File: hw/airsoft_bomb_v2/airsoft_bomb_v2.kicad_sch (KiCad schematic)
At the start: 43 parts, among them J1 Conn_01x10_Pin, J2 Conn_01x16_Pin, J3 BTN_R, J4 BTN_Y, J5 SIREN, J6 Conn_01x02_Socket, Q2 AO3400A, Q4 AO3400A, Q5 AO3400A, U1 PCF8574, U2 PCF8574, U4 LM317_SOT-223

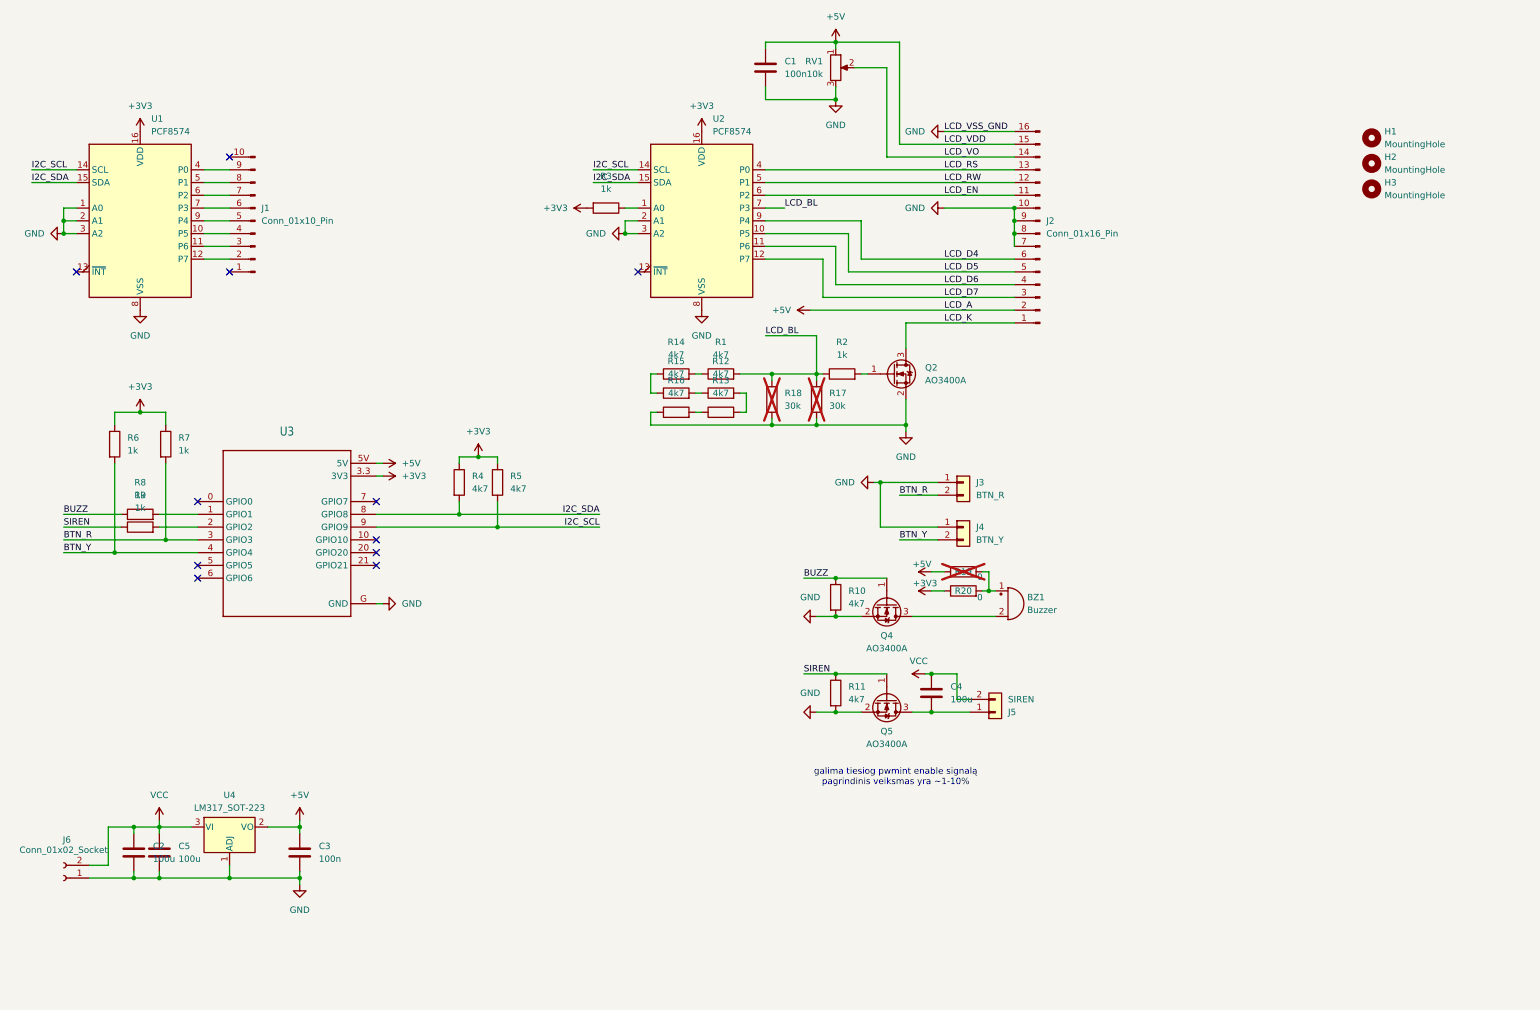
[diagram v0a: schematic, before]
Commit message: add kibot.sh and required fixes
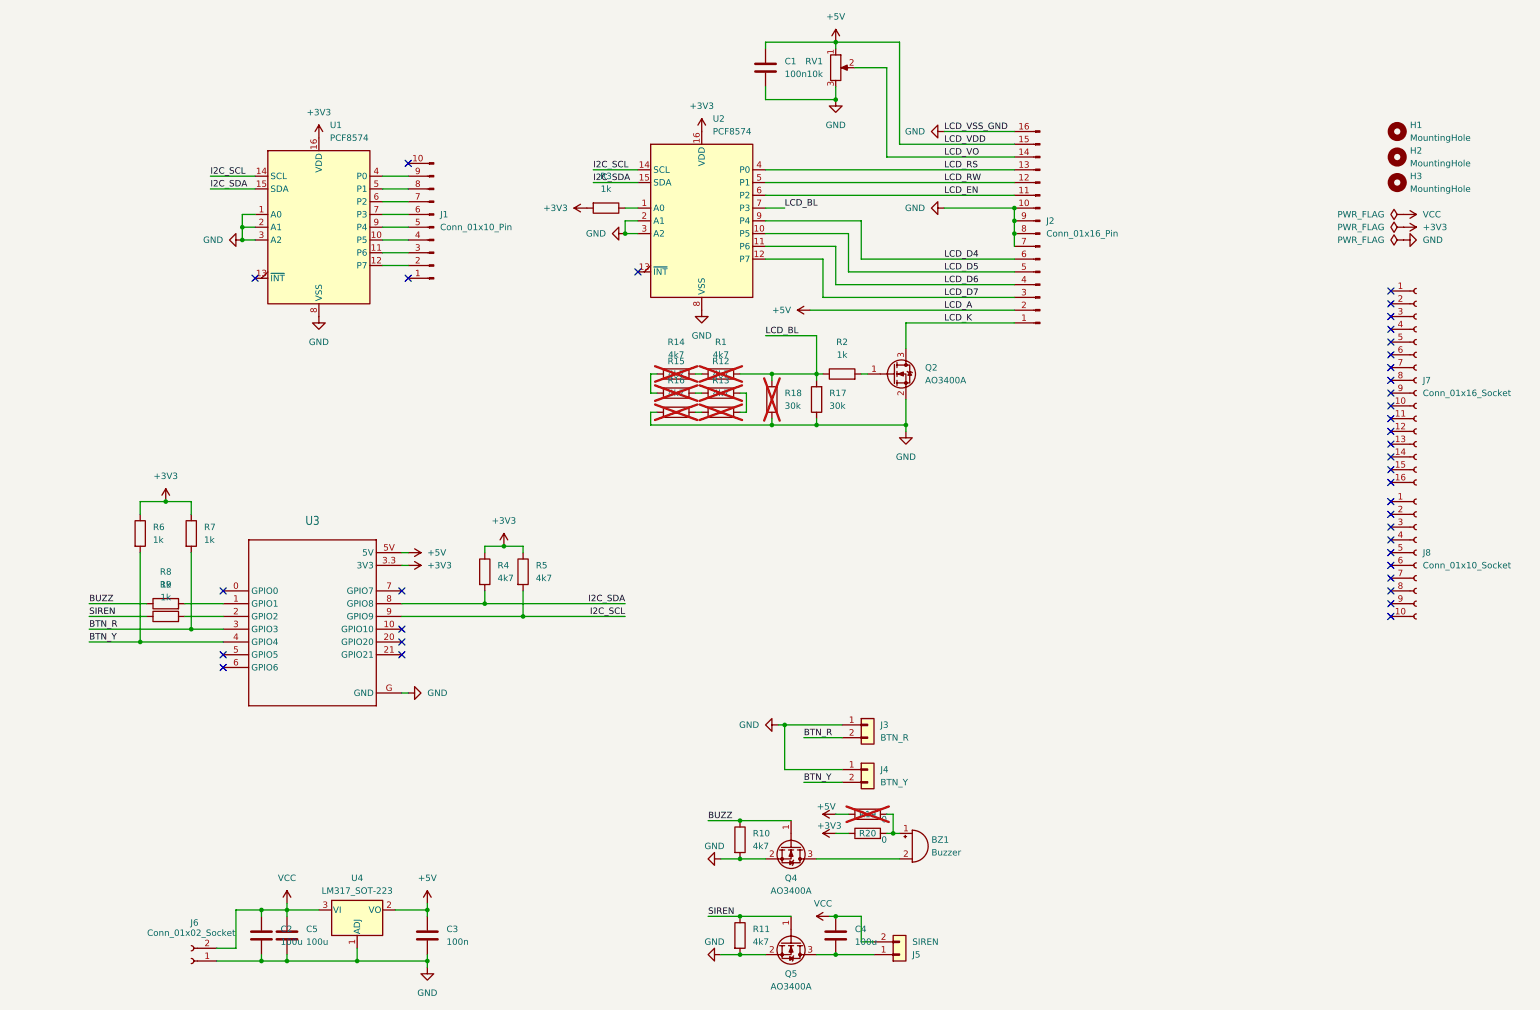
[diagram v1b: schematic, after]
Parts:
- added J7: Conn_01x16_Socket, Connector_PinHeader_2.54mm:PinHeader_1x16_P2.54mm_Horizontal, symbol Connector:Conn_01x16_Socket
- added J8: Conn_01x10_Socket, Connector_PinHeader_2.54mm:PinHeader_1x10_P2.54mm_Horizontal, symbol Connector:Conn_01x10_Socket
- R1, R12, R13, R14, R15, R16: now not fitted; now left out of the parts list
- R17: now fitted; now in the parts list
- R19: now left out of the parts list
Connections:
- no-connect marks 11 -> 37
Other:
- note removed: "galima tiesiog pwmint enable signalą pagrindinis veiksmas yra ~1-10%"
- moved on the sheet: BZ1, C2, C3, C4, C5, H1, H2, H3, J1, J3, J4, J5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

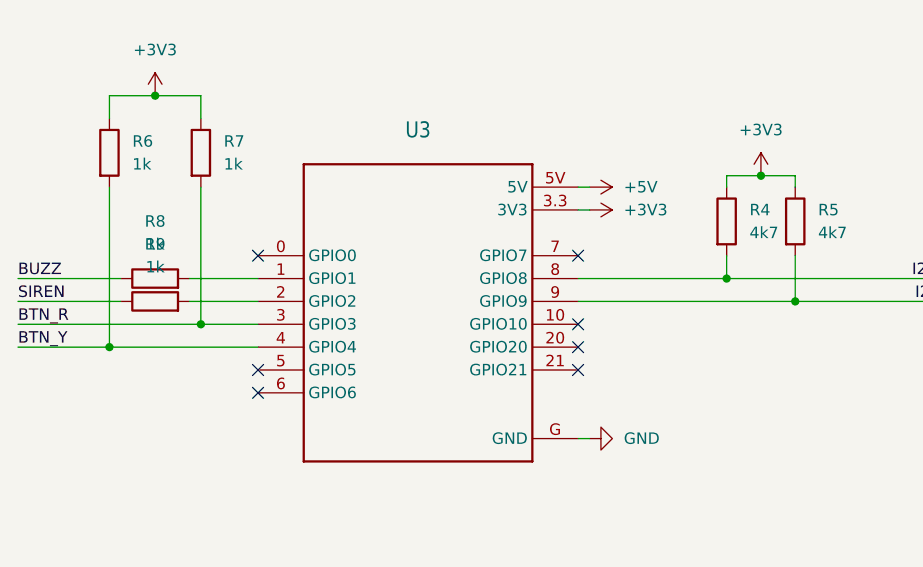
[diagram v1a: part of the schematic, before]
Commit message: move siren pin to something that is not high on boot
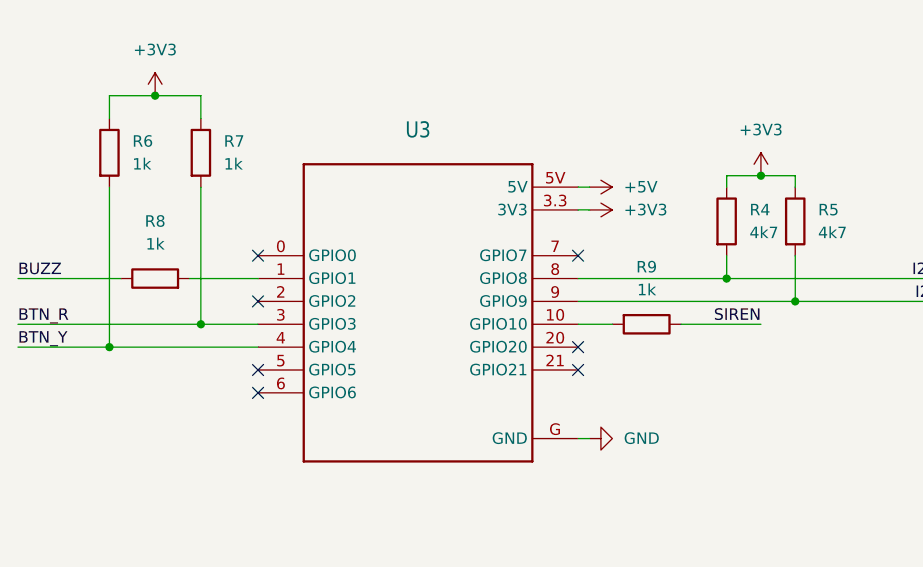
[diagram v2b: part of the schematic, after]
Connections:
- net at R9.2: now also U3.10 (GPIO10); no longer U3.2 (GPIO2)
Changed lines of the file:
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@@
 	)
 	(no_connect
-		(at 105.41 153.67)
-	)
-	(no_connect
 		(at 69.85 158.75)
 	)
@@
 	)
 	(no_connect
+		(at 69.85 151.13)
+	)
+	(no_connect
 		(at 302.26 116.84)
 	)
@@
 	(wire
 		(pts
+			(xy 116.84 153.67) (xy 125.73 153.67)
+		)
+		(stroke
+			(width 0)
+			(type default)
+		)
+	)
+	(wire
+		(pts
 			(xy 227.33 74.93) (xy 227.33 77.47)
 		)
@@
 	(wire
 		(pts
+			(xy 105.41 153.67) (xy 109.22 153.67)
+		)
+		(stroke
+			(width 0)
+			(type default)
+		)
+	)
+	(wire
+		(pts
 			(xy 149.86 148.59) (xy 121.92 148.59)
 		)
@@
 	(wire
 		(pts
-			(xy 43.18 151.13) (xy 54.61 151.13)
-		)
-		(stroke
-			(width 0)
-			(type default)
-		)
-	)
-	(wire
-		(pts
 			(xy 43.18 156.21) (xy 53.34 156.21)
 		)
@@
 	(wire
 		(pts
-			(xy 62.23 151.13) (xy 69.85 151.13)
-		)
-		(stroke
-			(width 0)
-			(type default)
-		)
-	)
-	(wire
-		(pts
 			(xy 196.85 215.9) (xy 199.39 215.9)
 		)
@@
 		)
 	)
+	(label "SIREN"
+		(at 125.73 153.67 180)
+		(effects
+			(font
+				(size 1.27 1.27)
+			)
+			(justify right bottom)
+		)
+	)
 	(label "I2C_SDA"
 		(at 67.31 66.04 0)
@@
 		)
 	)
-	(label "SIREN"
-		(at 43.18 151.13 0)
-		(effects
-			(font
-				(size 1.27 1.27)
-			)
-			(justify left bottom)
-		)
-	)
 	(label "BTN_Y"
 		(at 185.42 184.15 0)
@@
 	)
 	(symbol
-		(lib_id "Device:R")
-		(at 58.42 151.13 90)
-		(unit 1)
-		(exclude_from_sim no)
-		(in_bom yes)
-		(on_board yes)
-		(dnp no)
-		(fields_autoplaced yes)
-		(property "Reference" "R9"
-			(at 58.42 144.78 90)
-			(effects
-				(font
-					(size 1.27 1.27)
-				)
-			)
-		)
-		(property "Value" "1k"
-			(at 58.42 147.32 90)
-			(effects
-				(font
-					(size 1.27 1.27)
-				)
-			)
-		)
-		(property "Footprint" "Resistor_SMD:R_0805_2012Metric_Pad1.20x1.40mm_HandSolder"
-			(at 58.42 152.908 90)
-			(effects
-				(font
-					(size 1.27 1.27)
-				)
-				(hide yes)
-			)
-		)
-		(property "Datasheet" "~"
-			(at 58.42 151.13 0)
-			(effects
-				(font
-					(size 1.27 1.27)
-				)
-				(hide yes)
-			)
-		)
-		(property "Description" "Resistor"
-			(at 58.42 151.13 0)
-			(effects
-				(font
-					(size 1.27 1.27)
-				)
-				(hide yes)
-			)
-		)
-		(pin "2"
-		)
-		(pin "1"
-		)
-		(instances
-			(project "airsoft_bomb_v2"
-				(path "/57bad168-84d4-400d-bfdf-e1c1b50005bc"
-					(reference "R9")
-					(unit 1)
-				)
-			)
-		)
-	)
-	(symbol
 		(lib_id "Connector:Conn_01x10_Socket")
 		(at 307.34 138.43 0)
@@
 					(unit 1)
 				)
+			)
+		)
+	)
+	(symbol
+		(lib_id "Device:R")
+		(at 113.03 153.67 270)
+		(unit 1)
+		(exclude_from_sim no)
+		(in_bom yes)
+		(on_board yes)
+		(dnp no)
+		(fields_autoplaced yes)
+		(property "Reference" "R9"
+			(at 113.03 147.32 90)
+			(effects
+				(font
+					(size 1.27 1.27)
+				)
+			)
+		)
+		(property "Value" "1k"
+			(at 113.03 149.86 90)
+			(effects
+				(font
+					(size 1.27 1.27)
+				)
+			)
+		)
+		(property "Footprint" "Resistor_SMD:R_0805_2012Metric_Pad1.20x1.40mm_HandSolder"
+			(at 113.03 151.892 90)
+			(effects
+				(font
+					(size 1.27 1.27)
+				)
+				(hide yes)
+			)
+		)
+		(property "Datasheet" "~"
+			(at 113.03 153.67 0)
+			(effects
+				(font
+					(size 1.27 1.27)
+				)
+				(hide yes)
+			)
+		)
+		(property "Description" "Resistor"
+			(at 113.03 153.67 0)
+			(effects
+				(font
+					(size 1.27 1.27)
+				)
+				(hide yes)
+			)
+		)
+		(pin "2"
+		)
+		(pin "1"
+		)
+		(instances
+			(project "airsoft_bomb_v2"
+				(path "/57bad168-84d4-400d-bfdf-e1c1b50005bc"
+					(reference "R9")
+					(unit 1)
+				)

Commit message: change potentiometer to smd
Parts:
- RV1: footprint Potentiometer_THT:Potentiometer_Bourns_3296W_Vertical -> !custom:Potentiometer_Bourns_TC33X_Vertical
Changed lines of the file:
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@@
 			)
 		)
-		(property "Footprint" "Potentiometer_THT:Potentiometer_Bourns_3296W_Vertical"
+		(property "Footprint" "!custom:Potentiometer_Bourns_TC33X_Vertical"
 			(at 191.77 41.91 0)
 			(effects

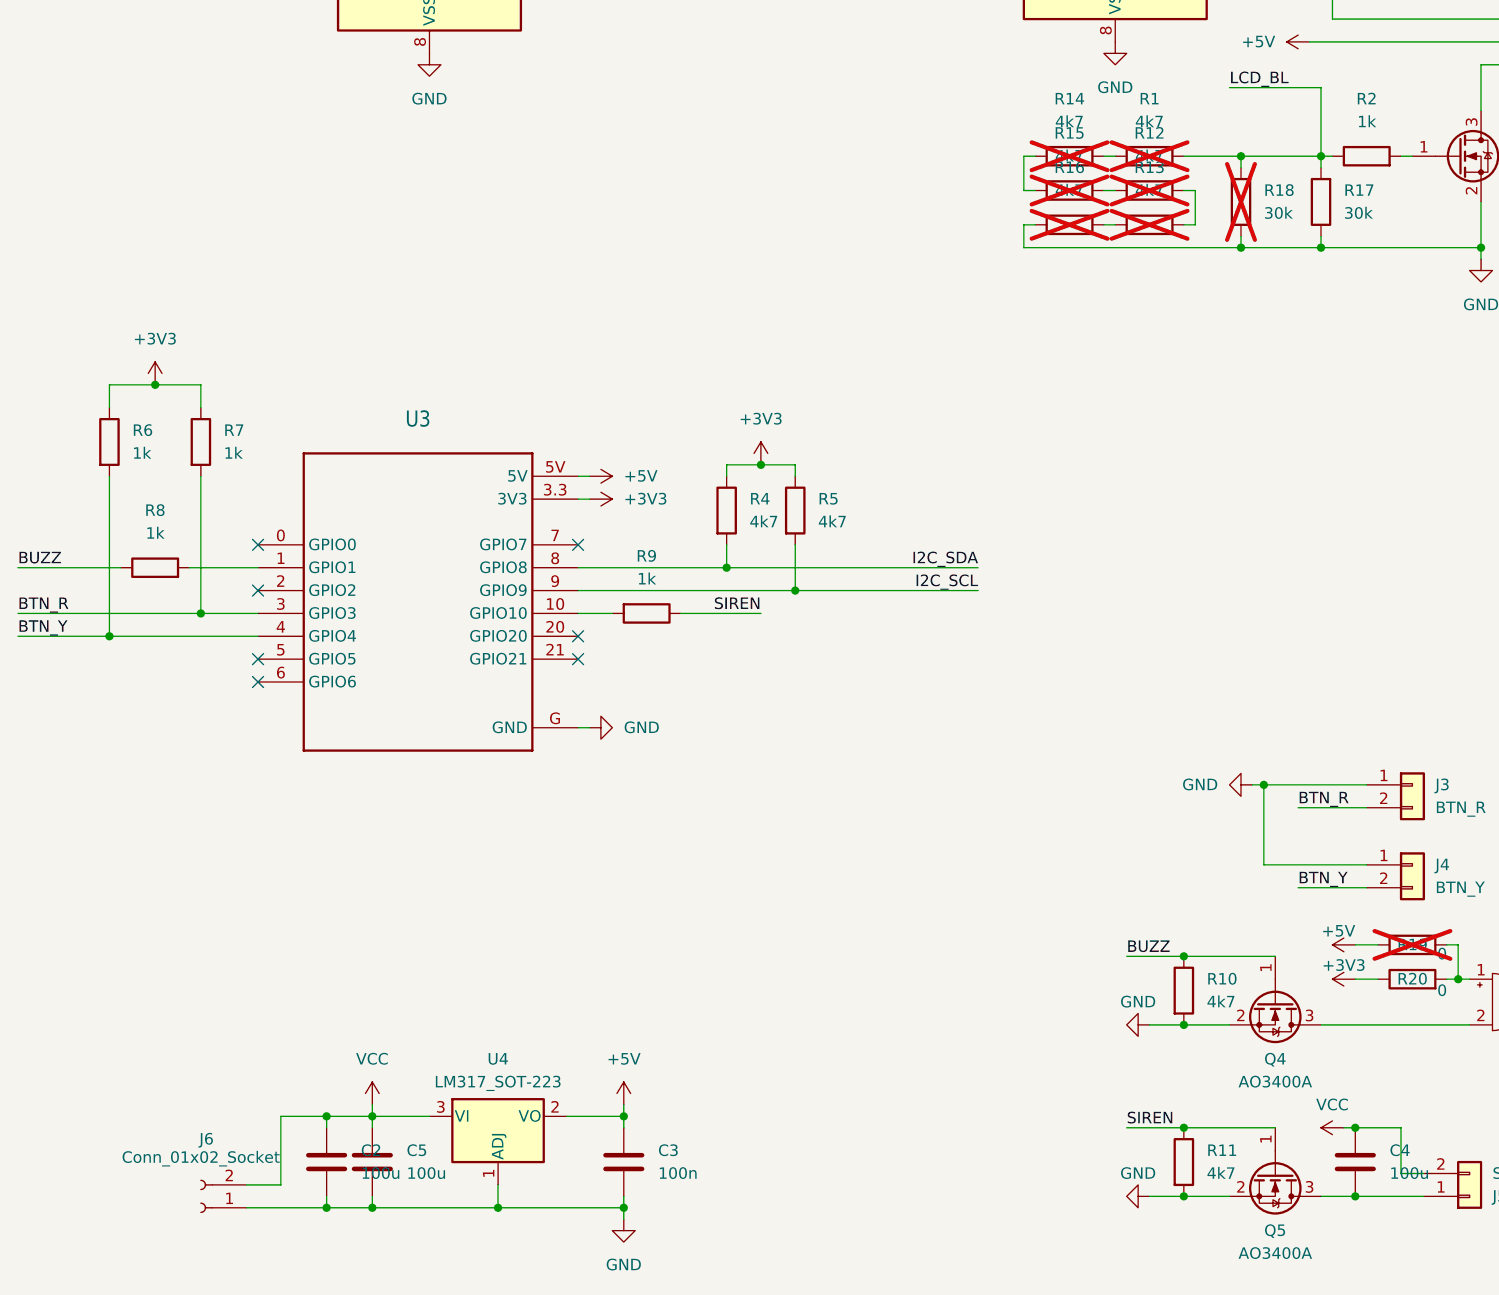
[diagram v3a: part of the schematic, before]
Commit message: add polarity protection diode on voltage input lcsc part numbers
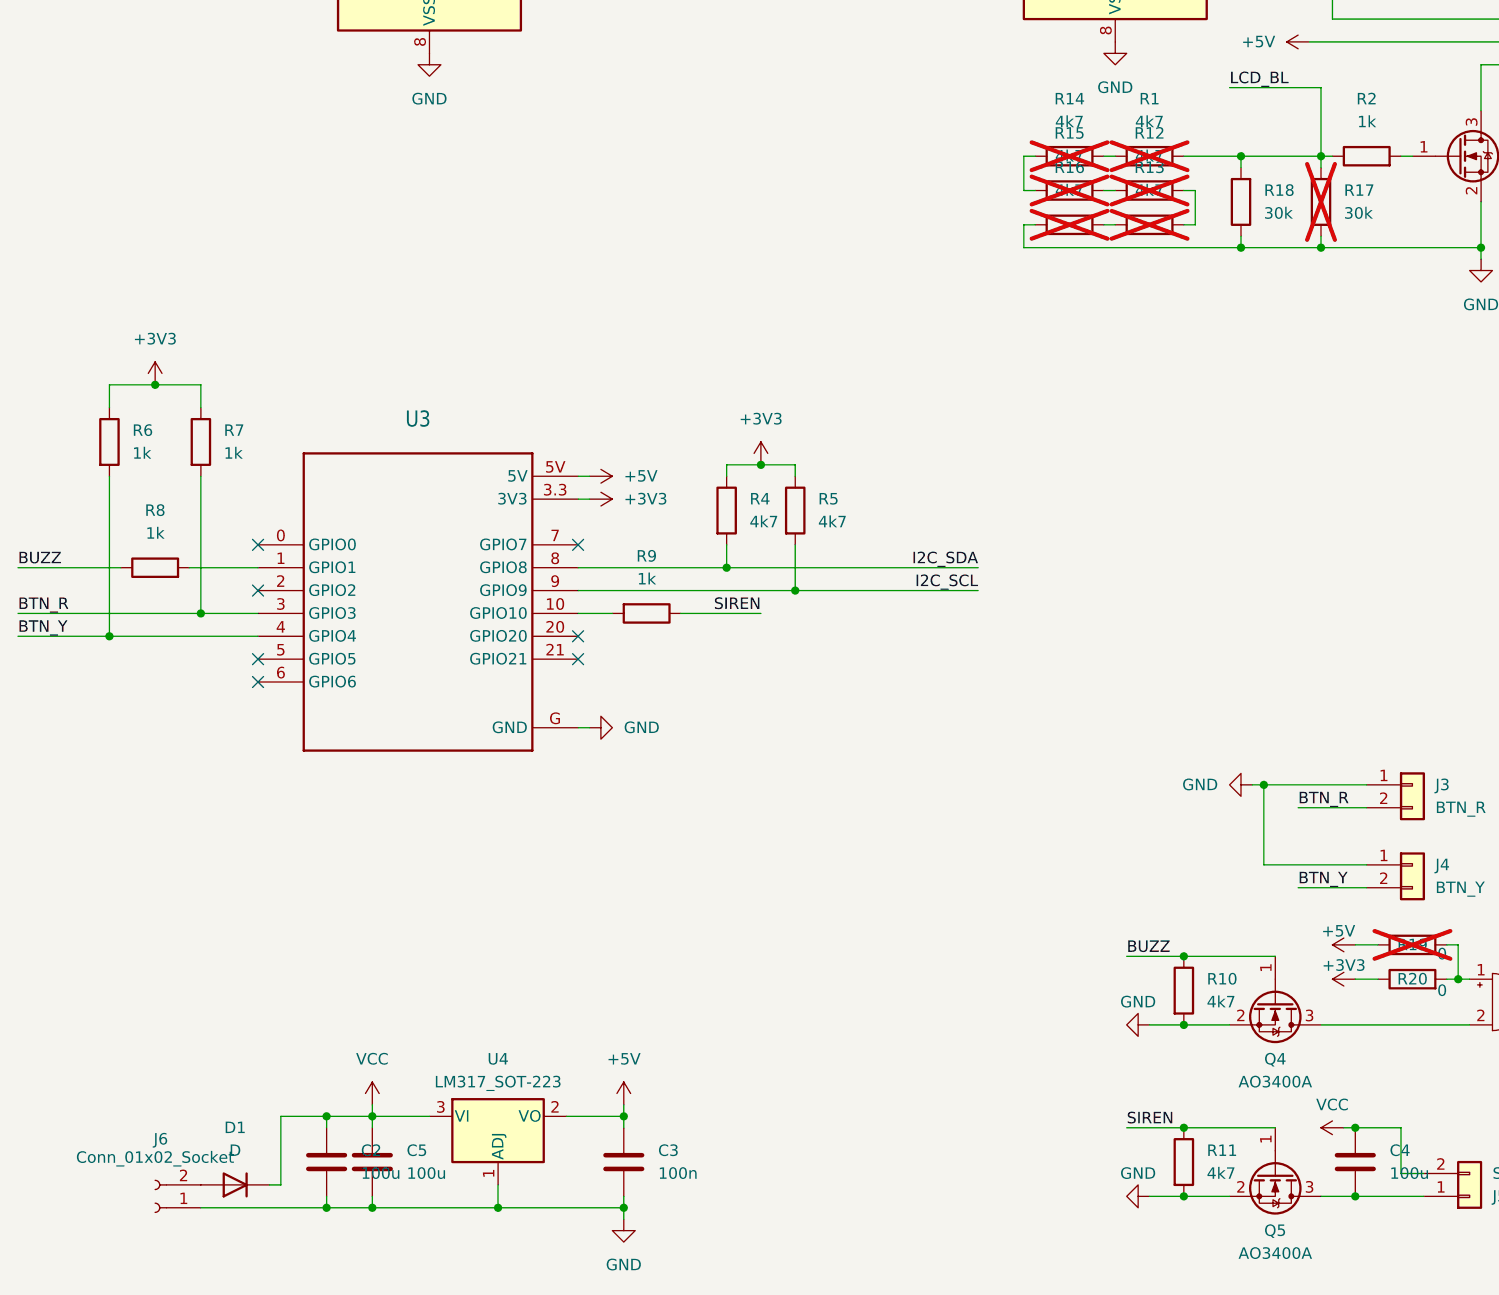
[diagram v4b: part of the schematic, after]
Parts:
- added D1: D, Diode_SMD:D_SOD-123, symbol Device:D
- C1, C3: MPN (none) -> C49678
- C2, C4, C5: MPN (none) -> C7432784
- Q2, Q4, Q5: MPN (none) -> C8545
- R1, R10, R11, R12, R13, R14, R15, R16, R4, R5: MPN (none) -> C17673
- R17: now not fitted; now left out of the parts list
- R18: MPN (none) -> C17621; now fitted; now in the parts list
- R19, R20: MPN (none) -> C17477
- R2, R3, R6, R7, R8, R9: MPN (none) -> C17513
- RV1: MPN (none) -> C719176
- U1, U2: MPN (none) -> C7605
- U4: MPN (none) -> C6187
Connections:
- net VCC: now also D1.1 (K); no longer J6.2 (Pin_2)
- new net: D1.2 (A), J6.2 (Pin_2)
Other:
- moved on the sheet: J6
